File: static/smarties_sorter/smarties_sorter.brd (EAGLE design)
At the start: 160 x 100 mm, 13 parts, among them IC1 MEGA8-P, Q1 16Mhz, Q2 IRLZ44Z

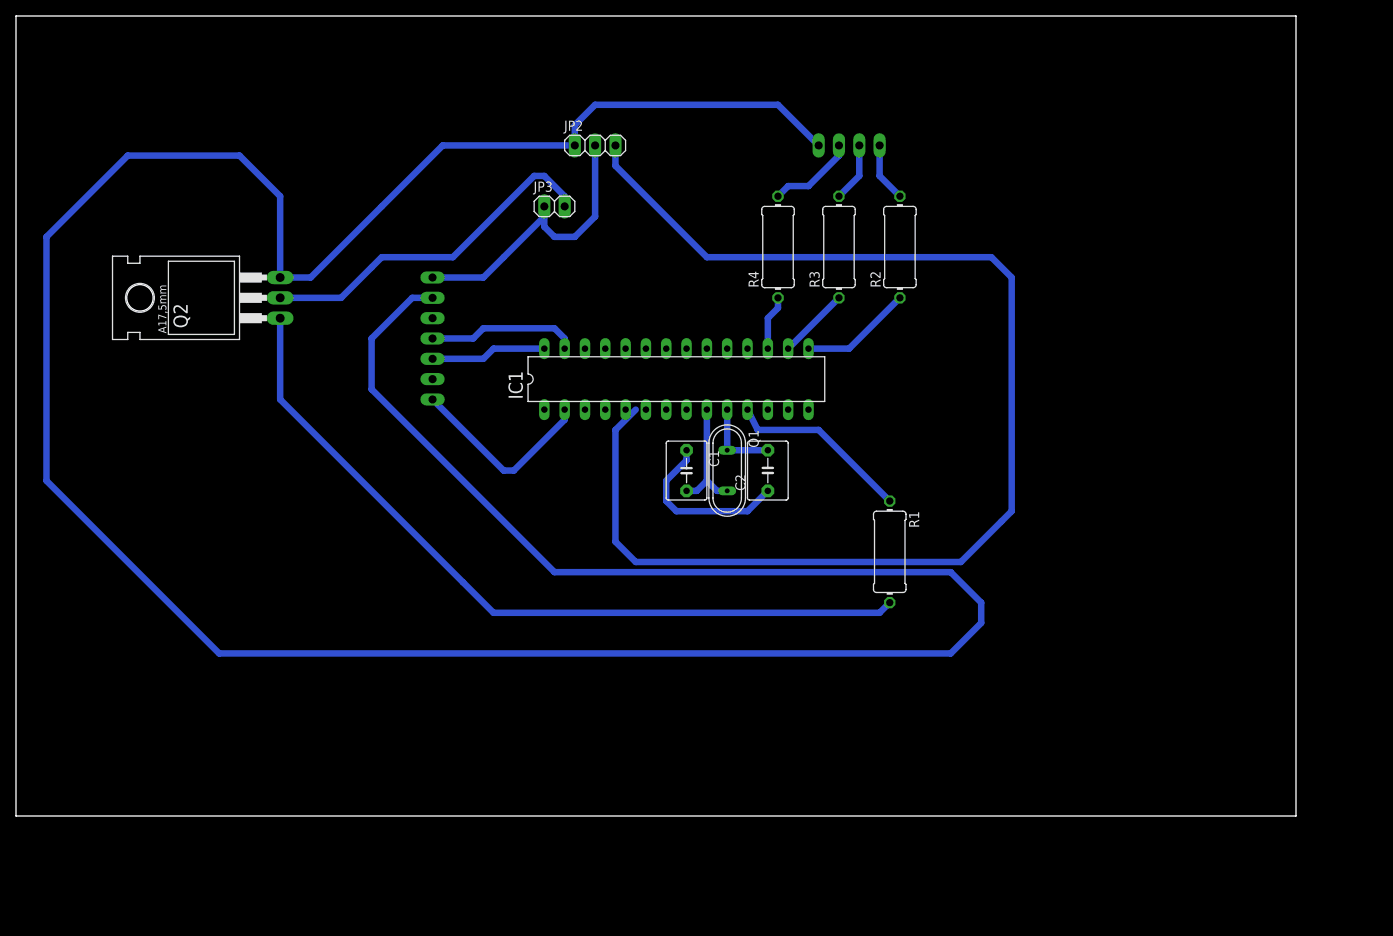
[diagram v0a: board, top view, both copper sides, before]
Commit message: [Smarties_sorter] Adds flyback diode
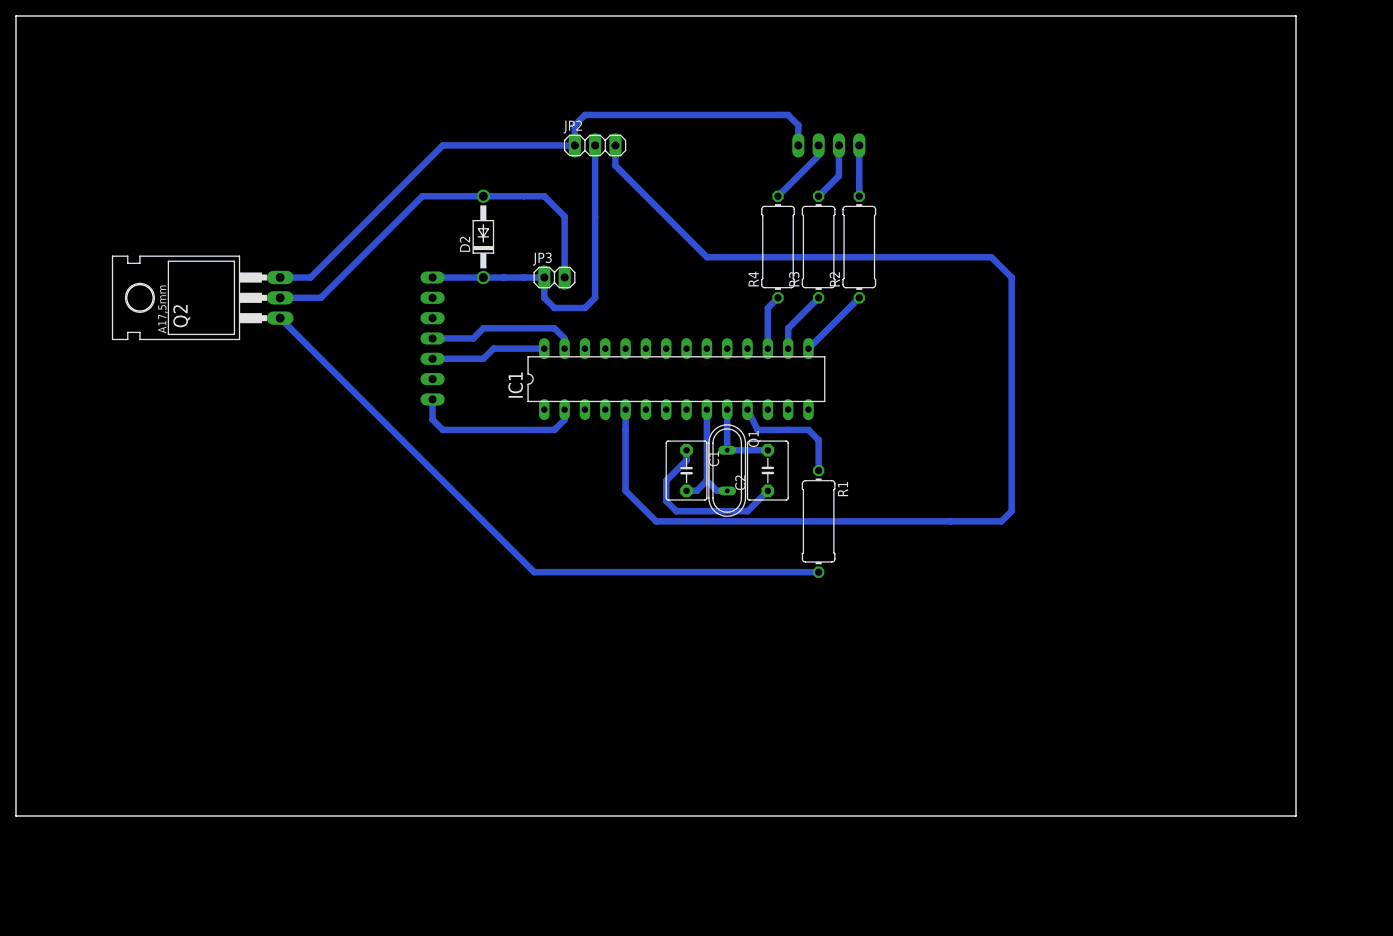
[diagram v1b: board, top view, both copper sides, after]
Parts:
- added D2: 1N4933, diode:DO41-10
- moved R1 9.67 mm to (100.3, 36.8)
- moved JP3 8.89 mm to (67.3, 67.3)
- moved R2 5.08 mm to (105.4, 71.1)
- moved JP1 2.54 mm to (101.6, 83.8)
- moved R3 2.54 mm to (100.3, 71.1)
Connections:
- net 5V: now also D2.C
- net N$7: now also D2.A
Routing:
- net GND: track 410.9 -> 99.4 mm
- net N$8: track 97.9 -> 80.5 mm
- net N$6: track 157.8 -> 147.6 mm
- net N$9: track 23.0 -> 14.8 mm
- net N$7: track 44.2 -> 49.5 mm
- net 5V: track 37.8 -> 43.0 mm
- net N$4: track 14.1 -> 8.98 mm
- net N$15: track 24.1 -> 21.4 mm
- net N$12: track 11.0 -> 8.45 mm
- net N$3: track 8.98 -> 7.93 mm
- net N$5: track 7.40 -> 6.35 mm

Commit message: [Smarties Sorter] Adds a buck
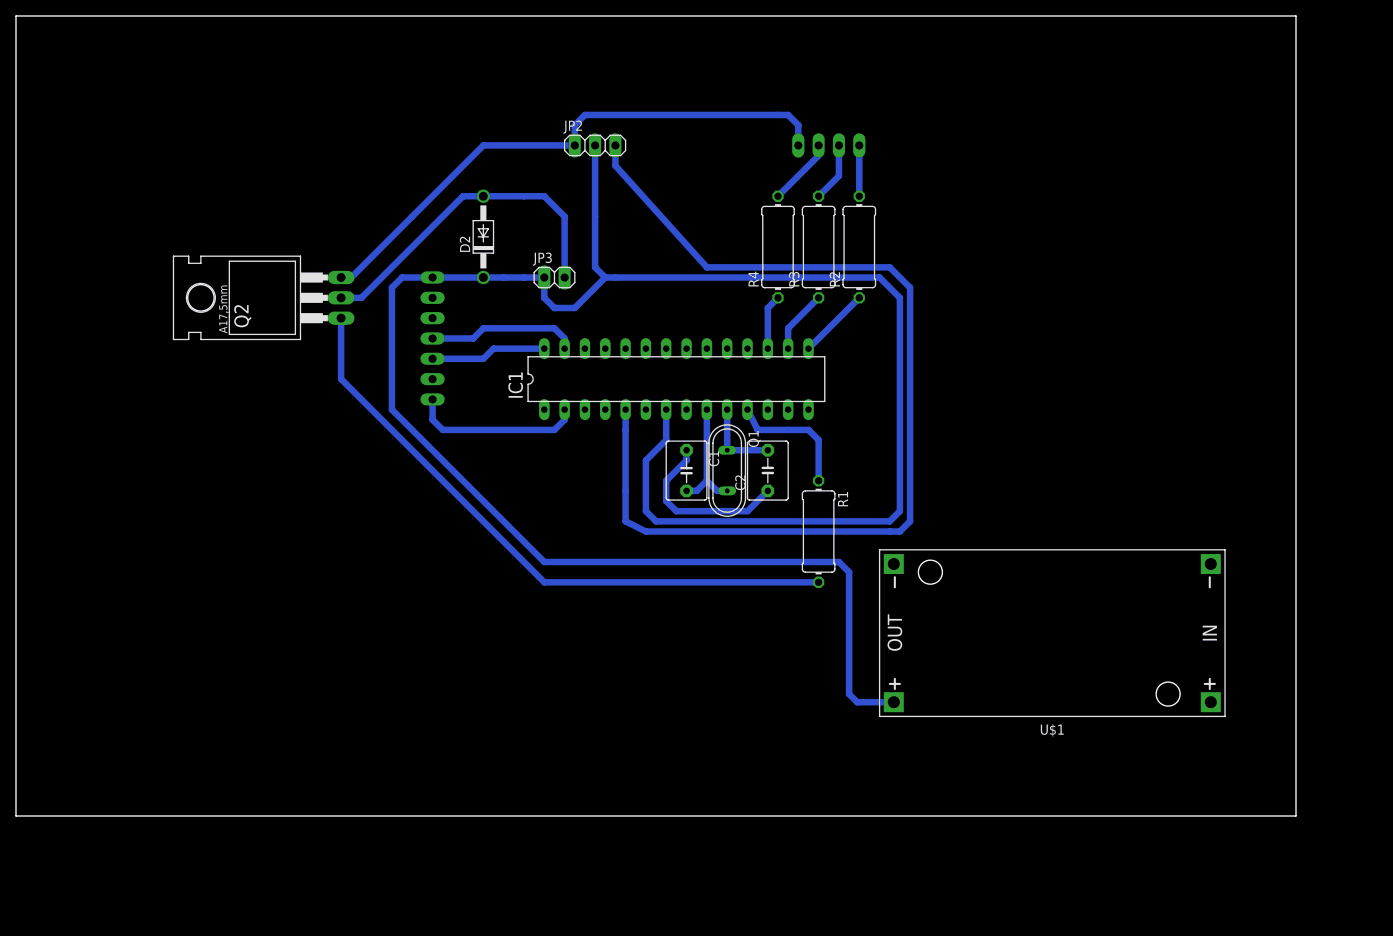
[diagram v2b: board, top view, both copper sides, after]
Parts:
- added U$1: DC-DC-STEP-DOWN-LM2596, diy-modules:DC-DC-STEP-DOWN-LM2596
- moved Q2 7.62 mm to (34.3, 64.8)
- moved R1 1.27 mm to (100.3, 35.6)
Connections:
- removed net VCC: IC1.7
- new net 12V: U$1.IN+
- new net 12V_GND: U$1.IN-
- net 5V: now also IC1.7, U$1.OUT+
- net GND: now also U$1.OUT-
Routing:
- net 5V: track 43.0 -> 262.0 mm
- net N$6: track 147.6 -> 125.6 mm
- net GND: track 99.4 -> 91.8 mm
- net N$7: track 49.5 -> 41.9 mm
- net N$8: track 80.5 -> 77.8 mm
- net N$9: track 14.8 -> 16.1 mm
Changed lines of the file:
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@@
 <element name="JP1" library="pinhead" package="1X04" value="" x="101.6" y="83.82" rot="MR0"/>
 <element name="JP2" library="pinhead" package="1X03" value="" x="72.39" y="83.82"/>
-<element name="Q2" library="transistor-power" package="TO220BH" value="IRLZ44Z" x="26.67" y="64.77" rot="R90"/>
+<element name="Q2" library="transistor-power" package="TO220BH" value="IRLZ44Z" x="34.29" y="64.77" rot="R90"/>
 <element name="JP3" library="pinhead" package="1X02" value="" x="67.31" y="67.31"/>
-<element name="R1" library="resistor" package="0411/12" value="1k" x="100.33" y="36.83" rot="R270"/>
+<element name="R1" library="resistor" package="0411/12" value="1k" x="100.33" y="35.56" rot="R270"/>
 <element name="R2" library="resistor" package="0411/12" value="180" x="105.41" y="71.12" rot="R90"/>
 <element name="R3" library="resistor" package="0411/12" value="100" x="100.33" y="71.12" rot="R90"/>
@@
 <element name="JP4" library="pinhead" package="1X07" value="" x="52.07" y="59.69" rot="MR270"/>
 <element name="D2" library="diode" package="DO41-10" value="1N4933" x="58.42" y="72.39" rot="R90"/>
+<element name="U$1" library="diy-modules" package="DC-DC-STEP-DOWN-LM2596" value="DC-DC-STEP-DOWN-LM2596" x="129.54" y="22.86" rot="R180"/>
 </elements>
 <signals>
@@
 <contactref element="JP1" pad="4"/>
 <contactref element="JP4" pad="2"/>
-<wire x1="33.02" y1="67.31" x2="36.83" y2="67.31" width="0.8128" layer="16"/>
-<wire x1="36.83" y1="67.31" x2="45.72" y2="76.2" width="0.8128" layer="16"/>
-<wire x1="45.72" y1="76.2" x2="53.34" y2="83.82" width="0.8128" layer="16"/>
-<wire x1="53.34" y1="83.82" x2="69.85" y2="83.82" width="0.8128" layer="16"/>
+<wire x1="40.64" y1="67.31" x2="41.91" y2="67.31" width="0.8128" layer="16"/>
+<wire x1="41.91" y1="67.31" x2="49.53" y2="74.93" width="0.8128" layer="16"/>
+<wire x1="49.53" y1="74.93" x2="58.42" y2="83.82" width="0.8128" layer="16"/>
+<wire x1="58.42" y1="83.82" x2="69.85" y2="83.82" width="0.8128" layer="16"/>
 <wire x1="69.85" y1="83.82" x2="69.85" y2="86.36" width="0.8128" layer="16"/>
 <wire x1="69.85" y1="86.36" x2="71.12" y2="87.63" width="0.8128" layer="16"/>
@@
 <wire x1="96.52" y1="87.63" x2="97.79" y2="86.36" width="0.8128" layer="16"/>
 <wire x1="97.79" y1="86.36" x2="97.79" y2="83.82" width="0.8128" layer="16"/>
-<wire x1="83.82" y1="50.8" x2="81.28" y2="58.42" width="0" layer="19" extent="1-1"/>
-<wire x1="83.82" y1="45.72" x2="83.82" y2="50.8" width="0" layer="19" extent="1-1"/>
+<contactref element="U$1" pad="OUT-"/>
+<wire x1="93.98" y1="40.64" x2="109.728" y2="31.496" width="0" layer="19" extent="1-1"/>
+<wire x1="83.82" y1="50.8" x2="83.82" y2="45.72" width="0" layer="19" extent="1-1"/>
+<wire x1="81.28" y1="58.42" x2="83.82" y2="50.8" width="0" layer="19" extent="1-1"/>
 <wire x1="69.85" y1="83.82" x2="81.28" y2="58.42" width="0" layer="19" extent="1-1"/>
-<wire x1="52.07" y1="64.77" x2="45.72" y2="76.2" width="0" layer="19" extent="16-16"/>
-</signal>
-<signal name="VCC">
-<contactref element="IC1" pad="7"/>
+<wire x1="52.07" y1="64.77" x2="49.53" y2="74.93" width="0" layer="19" extent="16-16"/>
 </signal>
 <signal name="AVCC">
@@
 <contactref element="JP4" pad="1"/>
 <wire x1="72.39" y1="83.82" x2="72.39" y2="74.93" width="0.8128" layer="16"/>
-<wire x1="72.39" y1="74.93" x2="72.39" y2="64.77" width="0.8128" layer="16"/>
-<wire x1="72.39" y1="64.77" x2="71.12" y2="63.5" width="0.8128" layer="16"/>
-<wire x1="71.12" y1="63.5" x2="67.31" y2="63.5" width="0.8128" layer="16"/>
+<wire x1="71.12" y1="64.77" x2="69.85" y2="63.5" width="0" layer="19" extent="1-16"/>
+<wire x1="69.85" y1="63.5" x2="69.85" y2="63.5" width="0" layer="19" extent="1-16"/>
+<wire x1="69.85" y1="63.5" x2="67.31" y2="63.5" width="0.8128" layer="16"/>
 <wire x1="67.31" y1="63.5" x2="66.04" y2="64.77" width="0.8128" layer="16"/>
 <wire x1="66.04" y1="64.77" x2="66.04" y2="67.31" width="0.8128" layer="16"/>
@@
 <wire x1="58.42" y1="67.31" x2="52.07" y2="67.31" width="0.8128" layer="16"/>
 <contactref element="D2" pad="C"/>
+<contactref element="U$1" pad="OUT+"/>
+<contactref element="IC1" pad="7"/>
+<wire x1="109.728" y1="14.224" x2="105.156" y2="14.224" width="0.8128" layer="16"/>
+<wire x1="105.156" y1="14.224" x2="104.14" y2="15.24" width="0.8128" layer="16"/>
+<wire x1="104.14" y1="15.24" x2="104.14" y2="30.48" width="0.8128" layer="16"/>
+<wire x1="104.14" y1="30.48" x2="102.87" y2="31.75" width="0.8128" layer="16"/>
+<wire x1="102.87" y1="31.75" x2="66.04" y2="31.75" width="0.8128" layer="16"/>
+<wire x1="66.04" y1="31.75" x2="46.99" y2="50.8" width="0.8128" layer="16"/>
+<wire x1="46.99" y1="50.8" x2="46.99" y2="66.04" width="0.8128" layer="16"/>
+<wire x1="46.99" y1="66.04" x2="48.26" y2="67.31" width="0.8128" layer="16"/>
+<wire x1="48.26" y1="67.31" x2="52.07" y2="67.31" width="0.8128" layer="16"/>
+<wire x1="81.28" y1="50.8" x2="81.28" y2="46.99" width="0.8128" layer="16"/>
+<wire x1="81.28" y1="46.99" x2="78.74" y2="44.45" width="0.8128" layer="16"/>
+<wire x1="78.74" y1="44.45" x2="78.74" y2="38.1" width="0.8128" layer="16"/>
+<wire x1="78.74" y1="38.1" x2="80.01" y2="36.83" width="0.8128" layer="16"/>
+<wire x1="80.01" y1="36.83" x2="109.22" y2="36.83" width="0.8128" layer="16"/>
+<wire x1="109.22" y1="36.83" x2="110.49" y2="38.1" width="0.8128" layer="16"/>
+<wire x1="110.49" y1="38.1" x2="110.49" y2="64.77" width="0.8128" layer="16"/>
+<wire x1="110.49" y1="64.77" x2="107.95" y2="67.31" width="0.8128" layer="16"/>
+<wire x1="107.95" y1="67.31" x2="74.93" y2="67.31" width="0.8128" layer="16"/>
+<wire x1="74.93" y1="67.31" x2="73.66" y2="67.31" width="0.8128" layer="16"/>
+<wire x1="73.66" y1="67.31" x2="69.85" y2="63.5" width="0.8128" layer="16"/>
+<wire x1="73.66" y1="67.31" x2="72.39" y2="74.93" width="0" layer="19" extent="16-16"/>
+<wire x1="72.39" y1="74.93" x2="72.39" y2="68.58" width="0.8128" layer="16"/>
+<wire x1="72.39" y1="68.58" x2="73.66" y2="67.31" width="0.8128" layer="16"/>
 </signal>
 <signal name="N$6">
@@
 <contactref element="IC1" pad="5"/>
 <wire x1="74.93" y1="83.82" x2="74.93" y2="81.28" width="0.8128" layer="16"/>
-<wire x1="74.93" y1="81.28" x2="86.36" y2="69.85" width="0.8128" layer="16"/>
-<wire x1="86.36" y1="69.85" x2="121.92" y2="69.85" width="0.8128" layer="16"/>
-<wire x1="121.92" y1="69.85" x2="124.46" y2="67.31" width="0.8128" layer="16"/>
-<wire x1="124.46" y1="67.31" x2="124.46" y2="38.1" width="0.8128" layer="16"/>
-<wire x1="124.46" y1="38.1" x2="123.19" y2="36.83" width="0.8128" layer="16"/>
-<wire x1="123.19" y1="36.83" x2="116.84" y2="36.83" width="0.8128" layer="16"/>
-<wire x1="116.84" y1="36.83" x2="80.01" y2="36.83" width="0.8128" layer="16"/>
-<wire x1="80.01" y1="36.83" x2="76.2" y2="40.64" width="0.8128" layer="16"/>
+<wire x1="74.93" y1="81.28" x2="86.36" y2="68.58" width="0.8128" layer="16"/>
+<wire x1="86.36" y1="68.58" x2="109.22" y2="68.58" width="0.8128" layer="16"/>
+<wire x1="109.22" y1="68.58" x2="111.76" y2="66.04" width="0.8128" layer="16"/>
+<wire x1="111.76" y1="66.04" x2="111.76" y2="36.83" width="0.8128" layer="16"/>
+<wire x1="111.76" y1="36.83" x2="110.49" y2="35.56" width="0.8128" layer="16"/>
+<wire x1="110.49" y1="35.56" x2="109.22" y2="35.56" width="0.8128" layer="16"/>
+<wire x1="109.22" y1="35.56" x2="78.74" y2="35.56" width="0.8128" layer="16"/>
+<wire x1="78.74" y1="35.56" x2="76.2" y2="36.83" width="0.8128" layer="16"/>
+<wire x1="76.2" y1="36.83" x2="76.2" y2="40.64" width="0.8128" layer="16"/>
 <wire x1="76.2" y1="40.64" x2="76.2" y2="48.26" width="0.8128" layer="16"/>
 <wire x1="76.2" y1="48.26" x2="76.2" y2="50.8" width="0.8128" layer="16"/>
@@
 <wire x1="66.04" y1="77.47" x2="63.5" y2="77.47" width="0.8128" layer="16"/>
 <wire x1="63.5" y1="77.47" x2="58.42" y2="77.47" width="0.8128" layer="16"/>
-<wire x1="58.42" y1="77.47" x2="50.8" y2="77.47" width="0.8128" layer="16"/>
-<wire x1="50.8" y1="77.47" x2="38.1" y2="64.77" width="0.8128" layer="16"/>
-<wire x1="38.1" y1="64.77" x2="33.02" y2="64.77" width="0.8128" layer="16"/>
+<wire x1="58.42" y1="77.47" x2="55.88" y2="77.47" width="0.8128" layer="16"/>
+<wire x1="55.88" y1="77.47" x2="43.18" y2="64.77" width="0.8128" layer="16"/>
+<wire x1="43.18" y1="64.77" x2="40.64" y2="64.77" width="0.8128" layer="16"/>
 <contactref element="D2" pad="A"/>
 </signal>
@@
 <contactref element="Q2" pad="G"/>
 <contactref element="R1" pad="2"/>
-<wire x1="33.02" y1="62.23" x2="64.77" y2="30.48" width="0.8128" layer="16"/>
-<wire x1="64.77" y1="30.48" x2="100.33" y2="30.48" width="0.8128" layer="16"/>
+<wire x1="40.64" y1="62.23" x2="40.64" y2="54.61" width="0.8128" layer="16"/>
+<wire x1="40.64" y1="54.61" x2="66.04" y2="29.21" width="0.8128" layer="16"/>
+<wire x1="66.04" y1="29.21" x2="100.33" y2="29.21" width="0.8128" layer="16"/>
 </signal>
 <signal name="N$9">
@@
 <wire x1="96.52" y1="48.26" x2="99.06" y2="48.26" width="0.8128" layer="16"/>
 <wire x1="99.06" y1="48.26" x2="100.33" y2="46.99" width="0.8128" layer="16"/>
-<wire x1="100.33" y1="46.99" x2="100.33" y2="43.18" width="0.8128" layer="16"/>
+<wire x1="100.33" y1="46.99" x2="100.33" y2="41.91" width="0.8128" layer="16"/>
 </signal>
 <signal name="N$3">
@@
 <wire x1="68.58" y1="59.69" x2="68.58" y2="58.42" width="0.8128" layer="16"/>
 </signal>
+<signal name="12V">
+<contactref element="U$1" pad="IN+"/>
+</signal>
+<signal name="12V_GND">
+<contactref element="U$1" pad="IN-"/>
+</signal>
 </signals>
